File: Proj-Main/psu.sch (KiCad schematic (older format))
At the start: 124 parts, among them J1 METER, J3 T1A, J4 T1B, J5 T1C, J6 SENSE, J8 OUT+, J9 OUT-, Q1 BC856, Q10 BC856, Q11 PMP4201Y, Q12 MMBT3904, Q13 BC856, Q14 MMBT3904, Q15 PZT2222A, Q16 MMBT3904, Q17 TIP105, Q18 PMP4201Y, Q19 MMBT2907A, Q2 MMBT3904, Q20 MMBT2907A, Q21 MMBT2907A, Q22 MMBT3904, Q23 PMP4201Y, Q24 MMBT3904, Q3 PZT2222A, Q4 BC856, Q5 MMBT3906, Q6 MMBT3906, Q7 PMP4201Y, Q8 PMP4201Y, Q9 BC856

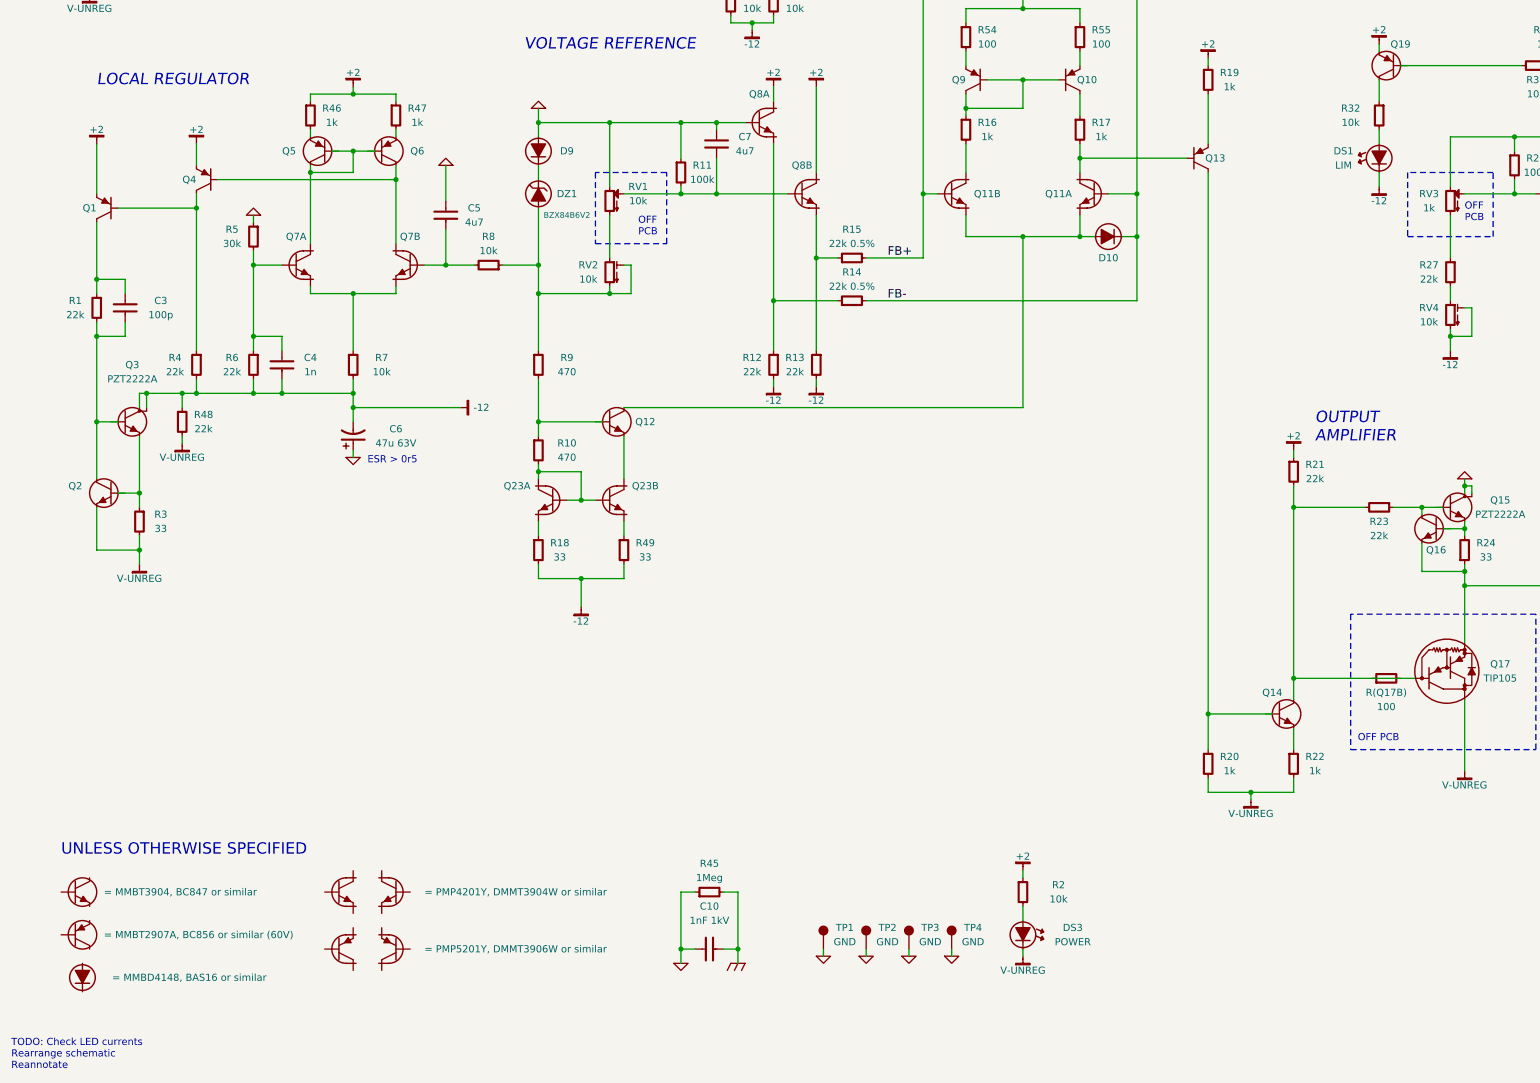
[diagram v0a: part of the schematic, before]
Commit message: Updated LED bias points
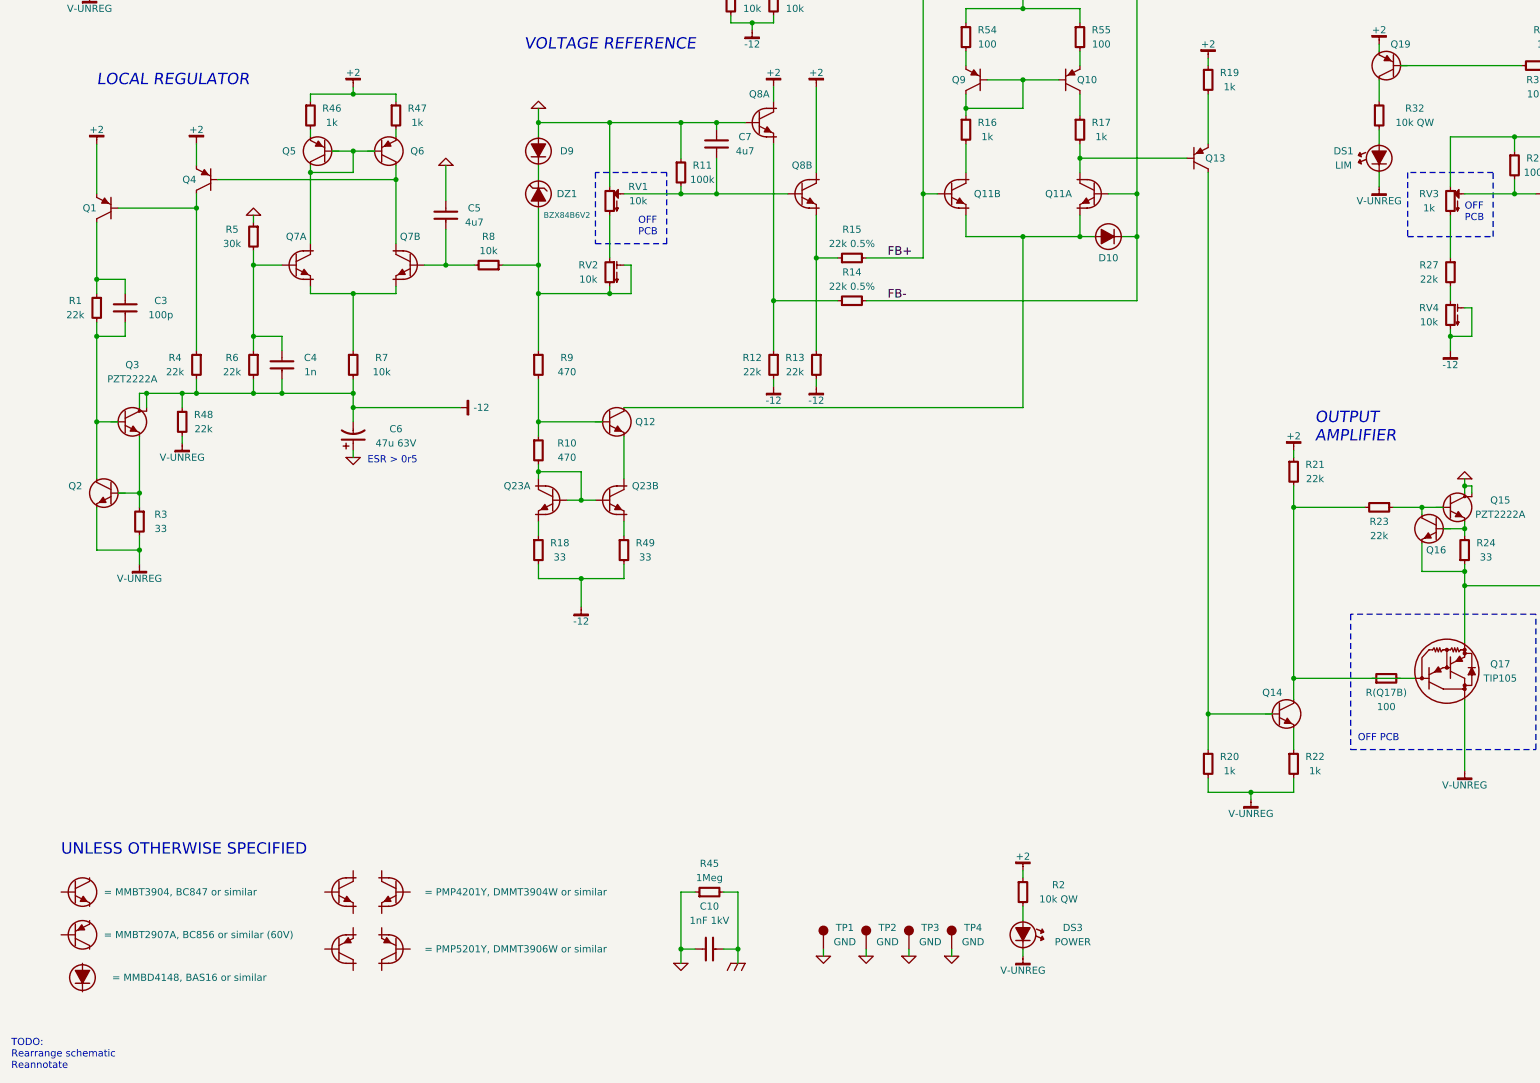
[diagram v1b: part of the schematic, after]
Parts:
- removed R2, R32: 10k, symbol R-0805
- added R2, R32: 10k QW, symbol R-1206
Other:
- note added: "TODO:\nRearrange schematic\nReannotate"
- note removed: "TODO: Check LED currents\nRearrange schematic\nReannotate"
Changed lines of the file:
@@
-$EndComp
-$Comp
-L R-0805 R32
-U 1 1 53228E7B
-P 10000 4150
-F 0 "R32" H 10200 4200 50  0000 C CNN
-F 1 "10k" H 10200 4100 50  0000 C CNN
-F 2 "" H 10000 4200 60  0000 C CNN
-F 3 "" H 10000 4200 60  0000 C CNN
-F 4 "RES 10k 5% [0805]" H 10000 4150 60  0001 C CNN "BomValueLine"
-F 5 "R32" H 10000 4150 50  0001 C CNN "OldReference"
-	1    10000 4150
-	-1   0    0    -1
 $EndComp
 $Comp
@@
 $EndComp
 $Comp
-L R-0805 R2
-U 1 1 532DFBBF
-P 7500 9600
-F 0 "R2" H 7750 9650 50  0000 C CNN
-F 1 "10k" H 7750 9550 50  0000 C CNN
-F 2 "" H 7500 9650 60  0000 C CNN
-F 3 "" H 7500 9650 60  0000 C CNN
-	1    7500 9600
-	1    0    0    -1
-$EndComp
-$Comp
 L V-UNREG #PWR018
 U 1 1 532DFBD3
@@
 $EndComp
 Text Notes 400  10850 0    50   ~ 0
-TODO: Check LED currents\nRearrange schematic\nReannotate
+TODO:\nRearrange schematic\nReannotate
 $Comp
 L PMP4201Y Q23
@@
 $EndComp
 $Comp
-L -12 #PWR043
-U 1 1 53675C12
-P 10000 4650
-F 0 "#PWR043" H 10000 4600 30  0001 C CNN
-F 1 "-12" H 10000 4550 50  0000 C CNN
-F 2 "" H 10000 4650 60  0000 C CNN
-F 3 "" H 10000 4650 60  0000 C CNN
-	1    10000 4650
-	1    0    0    -1
-$EndComp
-$Comp
-L +2 #PWR044
+L +2 #PWR043
 U 1 1 5367656E
 P 11900 4150
-F 0 "#PWR044" H 11900 4200 30  0001 C CNN
+F 0 "#PWR043" H 11900 4200 30  0001 C CNN
 F 1 "+2" H 11900 4250 50  0000 C CNN
 F 2 "" H 11900 4150 60  0000 C CNN
@@
 $EndComp
 $Comp
-L +2 #PWR045
+L +2 #PWR044
 U 1 1 53676808
 P 7500 9450
-F 0 "#PWR045" H 7500 9500 30  0001 C CNN
+F 0 "#PWR044" H 7500 9500 30  0001 C CNN
 F 1 "+2" H 7500 9550 50  0000 C CNN
 F 2 "" H 7500 9450 60  0000 C CNN
@@
 	1    0    0    -1
 $EndComp
+$Comp
+L R-1206 R2
+U 1 1 53679F03
+P 7500 9600
+F 0 "R2" H 7750 9650 50  0000 C CNN
+F 1 "10k QW" H 7750 9550 50  0000 C CNN
+F 2 "" H 7500 9650 60  0000 C CNN
+F 3 "" H 7500 9650 60  0000 C CNN
+	1    7500 9600
+	1    0    0    -1
+$EndComp
+$Comp
+L V-UNREG #PWR045
+U 1 1 5367A9F3
+P 10000 4650
+F 0 "#PWR045" H 10000 4600 30  0001 C CNN
+F 1 "V-UNREG" H 10000 4550 50  0000 C CNN
+F 2 "" H 10000 4650 60  0000 C CNN
+F 3 "" H 10000 4650 60  0000 C CNN
+	1    10000 4650
+	1    0    0    -1
+$EndComp
+$Comp
+L R-1206 R32
+U 1 1 5367B011
+P 10000 4150
+F 0 "R32" H 10250 4200 50  0000 C CNN
+F 1 "10k QW" H 10250 4100 50  0000 C CNN
+F 2 "" H 10000 4200 60  0000 C CNN
+F 3 "" H 10000 4200 60  0000 C CNN
+	1    10000 4150
+	1    0    0    -1
+$EndComp

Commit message: Rearranged schematic
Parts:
- C6: Value2 (none) -> ESR > 0r5
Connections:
- wire segments 281 -> 290
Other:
- note added: "ERROR\nAMPLIFIER"
- note removed: "Coupled\nto Q17"
- note removed: "ERROR AMPLIFIER"
- note removed: "ESR > 0r5"
- moved on the sheet: C1, C10, C2, C3, C4, C5, C6, C7, C8, C9, D1, D10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

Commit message: Reannotated schematic
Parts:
- DS3: OldReference DS1 -> DS3
- DZ2: renamed from DZ3; OldReference DZ1 -> DZ3
- J5: renamed from J6; OldReference (none) -> J6
- Q1: OldReference (none) -> Q1
- Q13: renamed from Q9; OldReference (none) -> Q9
- Q15: renamed from Q10; OldReference (none) -> Q10
- Q16: renamed from Q24; OldReference Q22 -> Q24
- Q17: renamed from Q13; OldReference (none) -> Q13
- Q4: OldReference (none) -> Q4
- Q8: renamed from Q23; OldReference Q8 -> Q23
- R14: renamed from R49; OldReference R18 -> R49
- R21: renamed from R50; OldReference R44 -> R50
- R23: renamed from R54; OldReference (none) -> R54
- R27: renamed from R51; OldReference (none) -> R51
- R28: renamed from R52; OldReference (none) -> R52
- R29: renamed from R55; OldReference (none) -> R55
- R3: renamed from R48; OldReference R4 -> R48
- R31: renamed from R53; OldReference R41 -> R53
- R37: renamed from R32; OldReference (none) -> R32
- R55: renamed from R2; OldReference (none) -> R2
- R7: renamed from R46; OldReference (none) -> R46
- R9: renamed from R47; OldReference (none) -> R47
- TP1: OldReference (none) -> TP1
- TP2: OldReference (none) -> TP2
- TP3: OldReference (none) -> TP3
- TP4: OldReference (none) -> TP4
- renumbered C3 to C1, C1 to C2, C4 to C3, C2 to C4, C6 to C5, C5 to C6, C9 to C8, C8 to C9, D12 to D11, D11 to D12, D3 to D2, D2 to D3, D8 to D7, D7 to D8, DS2 to DS1, DS1 to DS2, DZ2 to DZ3, J3 to J1, J4 to J2, J5 to J3, J8 to J4, J1 to J6, J9 to J7, Q8 to Q10, Q22 to Q11, Q11 to Q12, Q21 to Q14, Q14 to Q18, Q16 to Q20, Q17 to Q21, Q15 to Q22, Q18 to Q23, Q20 to Q24, Q7 to Q5, Q5 to Q6, Q6 to Q7, Q12 to Q9, R8 to R10, R9 to R11, R10 to R12, R18 to R13, R11 to R15, R12 to R16, R13 to R17, R15 to R18, R14 to R19, R3 to R2, R44 to R20, R43 to R22, R16 to R24, R42 to R25, R41 to R26, R17 to R30, R19 to R32, R20 to R33, R21 to R34, R22 to R35, R23 to R36, R24 to R38, R27 to R39, R26 to R40, R31 to R41, R29 to R42, R28 to R43, R25 to R44, R30 to R45, R34 to R46, R33 to R47, R45 to R48, R37 to R49, R38 to R50, R35 to R51, R40 to R52, R39 to R53, R36 to R54, R7 to R8
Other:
- note added: "E100A"
- note added: "E101A"
- note added: "E102A"
- note added: "R49"
- note added: "R50"
- note added: "R51"
- note added: "R54"
- note removed: "PS-1H"
- note removed: "PS-1L"
- note removed: "PS-1LL"
- note removed: "R33"
- note removed: "R35"
- note removed: "R36"
- note removed: "R37"
- note removed: "R38"
- note removed: "TODO:\nRearrange schematic\nReannotate"

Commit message: Frequency compensation
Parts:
- removed R21: 1k, symbol R-0805
- added C11: 1n, symbol C-0805
- added C12: 330p, symbol C-0805
- added R56, R57: 1k, symbol R-0805
- C1: value 100p -> 330p
- R20, R42: value 1k -> 2k
- R45: value 33 -> 1k
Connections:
- wire segments 290 -> 298
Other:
- moved on the sheet: DS2, Q19, R20, R34, R37, R39, R40, RV3, RV4

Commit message: PCB tweaks
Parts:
- C1, C12: value 330p -> 1n
- DZ1: value BZX84B6V2 -> 6v2; PartNo (none) -> BZX84-B6V2
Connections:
- wire segments 298 -> 426
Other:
- moved on the sheet: C1, C12, C7, C9, D11, D9, DS2, DZ1, DZ3, J7, Q1, Q19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

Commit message: Added guard traces, fixed overlapping components
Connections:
- net labels added: GUARD
- wire segments 426 -> 309

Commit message: Some PCB tweaks
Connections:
- wire segments 309 -> 433
